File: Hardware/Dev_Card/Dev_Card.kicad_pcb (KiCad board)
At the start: 2 copper layers, 75 x 116.7 mm, 52 parts, among them J1 CON1, J2 CON2, J3 CON3, U1 ProtoBoard, U2 CARD ?

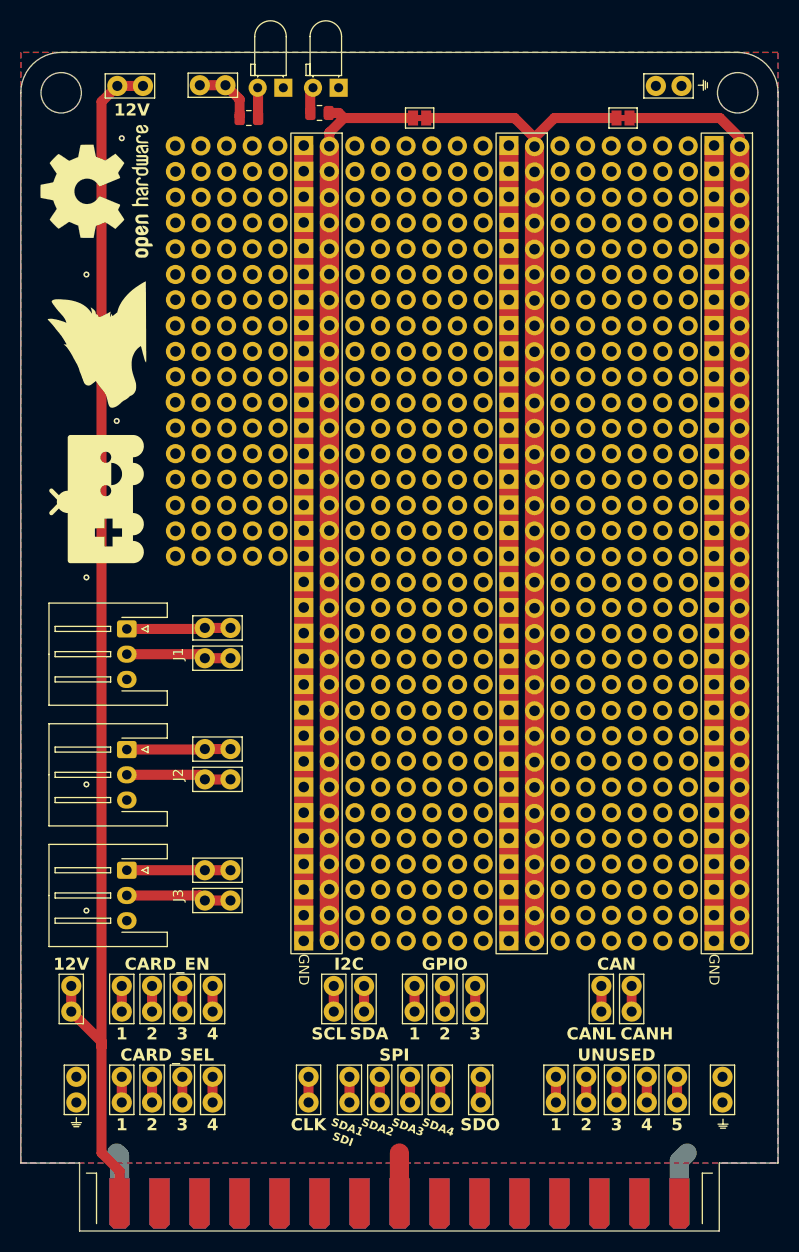
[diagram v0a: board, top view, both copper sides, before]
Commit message: Fix broken references
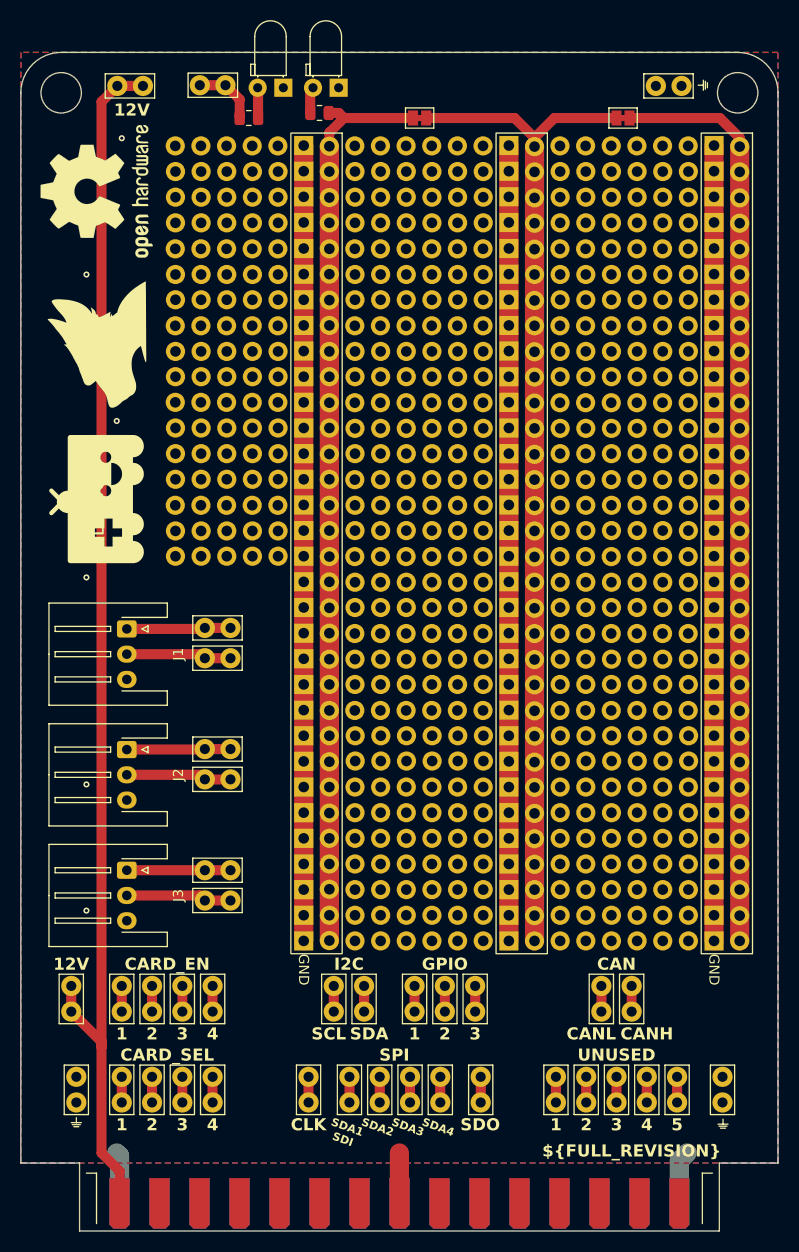
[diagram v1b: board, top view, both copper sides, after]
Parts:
- renumbered G*** to LOGO1, G*** to LOGO2, REF** to LOGO3
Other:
- board text added: "${FULL_REVISION}"
